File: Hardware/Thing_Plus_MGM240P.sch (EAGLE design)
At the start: 92 parts, among them J1 THING_PLUS_LOGICAL, J2 USB Female Type C Connector, J3 QWIIC_RIGHT_ANGLE, J5 MICRO-SDFRICTION, Q1 20V/4.2A/52mΩ/1.4W, U1 MGM240P, U2 XC6222B331MR-G, U3 EFM32GG12B410F1024GL120, U4 MCP73831, U5 MAX17048, U6 M24C02-FMC6TG, U7 MX25R8035FZUIL0, Y1 CRYSTAL-48MHZ

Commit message: Change debugger power circuitry
Remove VDDJ jumper
Remove VDDJ net and replace with 3V3
Add DBG_WAKE net and circuitry, which controls sleep state of debugger chip
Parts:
- removed VDDJ_EN: JUMPER-SMT_2_NC_TRACE_SILK, SparkFun-Jumpers:JUMPER-SMT_2_NC_TRACE_SILK
- added D8: 120mA/40V/370mV, SparkFun-DiscreteSemi:DIODE-SCHOTTKY-RB751S40
- added R18: 1k, SparkFun-Resistors:1KOHM-0402T-1/16W-1%
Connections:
- removed net VDDJ: C18.1, C19.1, C20.1, C21.1, C4.1, C5.1, C6.1, FB1.2, R1.2, R12.2, R14.2, R16.2, R17.2, TP1.1, U3D.DVDD, U3D.IOVDD0, U3D.IOVDD1, U6.VCC, U7.VCC, U7.WP, VDDJ_EN.1
- new net DBG_WAKE: D8.A, U3A.PA5, U3A.PA6
- net 3.3V: now also C18.1, C19.1, C20.1, C21.1, C4.1, C5.1, C6.1, FB1.2, R1.2, R12.2, R14.2, R16.2, R17.2, TP1.1, U3D.DVDD, U3D.IOVDD0, U3D.IOVDD1, U6.VCC, U7.VCC, U7.WP; no longer VDDJ_EN.2
- net GND: now also R18.1
- net V_USB: now also D8.C, R18.2
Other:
- note removed: "Cut trace to disabled debugger chip"

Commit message: Design review updates
Remove VDDJ label from silk
Add jumper to debugger power control circuit for USB battery applications
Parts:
- added LP: JUMPER-SMT_2_NC_TRACE_SILK, SparkFun-Jumpers:JUMPER-SMT_2_NC_TRACE_SILK
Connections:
- new net N$24: D8.C, LP.1, R18.2
- net DBG_WAKE: no longer U3A.PA5
- net V_USB: now also LP.2; no longer D8.C, R18.2
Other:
- note added: "Cut trace to force debugger into low power mode"
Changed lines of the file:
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@@
 <part name="SUPPLY53" library="SparkFun-PowerSymbols" deviceset="3.3V" device=""/>
 <part name="SUPPLY54" library="SparkFun-PowerSymbols" deviceset="3.3V" device=""/>
+<part name="LP" library="SparkFun-Jumpers" deviceset="JUMPER-SMT_2_NC_TRACE" device="_SILK" package3d_urn="urn:adsk.eagle:package:39281/1"/>
 </parts>
 <sheets>
@@
 <wire x1="88.9" y1="55.88" x2="88.9" y2="0" width="0.2032" layer="97" style="longdash"/>
 <wire x1="170.18" y1="55.88" x2="170.18" y2="0" width="0.2032" layer="97" style="longdash"/>
+<text x="312.42" y="195.58" size="2.032" layer="97" font="vector" align="center">Cut trace to force
+debugger into low
+power mode</text>
 </plain>
 <instances>
@@
 <attribute name="VALUE" x="298.704" y="177.8" size="1.778" layer="96" font="vector" rot="R90" align="top-center"/>
 </instance>
-<instance part="SUPPLY22" gate="G$1" x="297.18" y="187.96" smashed="yes">
-<attribute name="VALUE" x="297.18" y="190.754" size="1.778" layer="96" align="bottom-center"/>
+<instance part="SUPPLY22" gate="G$1" x="297.18" y="200.66" smashed="yes">
+<attribute name="VALUE" x="297.18" y="203.454" size="1.778" layer="96" align="bottom-center"/>
 </instance>
 <instance part="GND50" gate="1" x="297.18" y="167.64" smashed="yes">
@@
 <instance part="SUPPLY54" gate="G$1" x="218.44" y="30.48" smashed="yes">
 <attribute name="VALUE" x="218.44" y="33.274" size="1.778" layer="96" align="bottom-center"/>
+</instance>
+<instance part="LP" gate="G$1" x="297.18" y="193.04" smashed="yes" rot="R90">
+<attribute name="NAME" x="294.132" y="193.04" size="1.778" layer="95" font="vector" rot="R90" align="center"/>
 </instance>
 </instances>
@@
 </segment>
 <segment>
-<pinref part="R18" gate="G$1" pin="2"/>
-<wire x1="297.18" y1="182.88" x2="297.18" y2="185.42" width="0.1524" layer="91"/>
-<pinref part="D8" gate="G$1" pin="C"/>
-<wire x1="297.18" y1="185.42" x2="299.72" y2="185.42" width="0.1524" layer="91"/>
+<pinref part="LP" gate="G$1" pin="2"/>
 <pinref part="SUPPLY22" gate="G$1" pin="V_USB"/>
-<wire x1="297.18" y1="185.42" x2="297.18" y2="187.96" width="0.1524" layer="91"/>
-<junction x="297.18" y="185.42"/>
+<wire x1="297.18" y1="198.12" x2="297.18" y2="200.66" width="0.1524" layer="91"/>
 </segment>
 </net>
@@
 <net name="DBG_WAKE" class="0">
 <segment>
-<pinref part="U3" gate="A" pin="PA5"/>
-<wire x1="111.76" y1="104.14" x2="109.22" y2="104.14" width="0.1524" layer="91"/>
-<label x="109.22" y="104.14" size="1.27" layer="95" font="vector" rot="R180" xref="yes"/>
-</segment>
-<segment>
 <pinref part="D8" gate="G$1" pin="A"/>
 <wire x1="304.8" y1="185.42" x2="307.34" y2="185.42" width="0.1524" layer="91"/>
@@
 </segment>
 </net>
+<net name="N$24" class="0">
+<segment>
+<pinref part="R18" gate="G$1" pin="2"/>
+<pinref part="LP" gate="G$1" pin="1"/>
+<wire x1="297.18" y1="182.88" x2="297.18" y2="185.42" width="0.1524" layer="91"/>
+<pinref part="D8" gate="G$1" pin="C"/>
+<wire x1="297.18" y1="185.42" x2="297.18" y2="187.96" width="0.1524" layer="91"/>
+<wire x1="299.72" y1="185.42" x2="297.18" y2="185.42" width="0.1524" layer="91"/>
+<junction x="297.18" y="185.42"/>
+</segment>
+</net>

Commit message: Testing fixes
Update version number to v02
Mirror MX8035 footprint (whoops...)
Swap R15 for 2k2 (turns out VREGO is 3V3, not 5V)
Add trace to 3V3 pour to connect between V_USB and N$24
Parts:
- R15: value 4.7k -> 2.2k; device SparkFun-Resistors:4.7KOHM-0402T-1/16W-1% -> SparkFun-Resistors:2.2KOHM-0402T-1/16W-1%
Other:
- note added: "v02"
- note removed: "v01"
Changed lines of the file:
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@@
 <part name="SUPPLY34" library="SparkFun-PowerSymbols" deviceset="V_USB" device=""/>
 <part name="D6" library="SparkFun-LED" deviceset="LED-BLUE" device="0603" value="BLUE"/>
-<part name="R15" library="SparkFun-Resistors" deviceset="4.7KOHM" device="-0402T-1/16W-1%" value="4.7k"/>
+<part name="R15" library="SparkFun-Resistors" deviceset="2.2KOHM" device="-0402T-1/16W-1%" value="2.2k"/>
 <part name="C11" library="SparkFun-Capacitors" deviceset="1.0UF" device="-0402T-16V-10%" value="1.0uF"/>
 <part name="C12" library="SparkFun-Capacitors" deviceset="4.7UF" device="-0402_TIGHT-6.3V-20%-X5R" value="4.7uF"/>
@@
 <wire x1="99.06" y1="149.86" x2="0" y2="149.86" width="0.2032" layer="97" style="longdash"/>
 <text x="358.14" y="12.7" size="2.54" layer="94" font="vector" align="center">Dryw Wade</text>
-<text x="424.18" y="7.62" size="2.54" layer="94" font="vector" align="center">v01</text>
+<text x="424.18" y="7.62" size="2.54" layer="94" font="vector" align="center">v02</text>
 <text x="20.32" y="205.74" size="2.032" layer="97" font="vector" rot="R180" align="center">Cut trace to
 remove power LED</text>

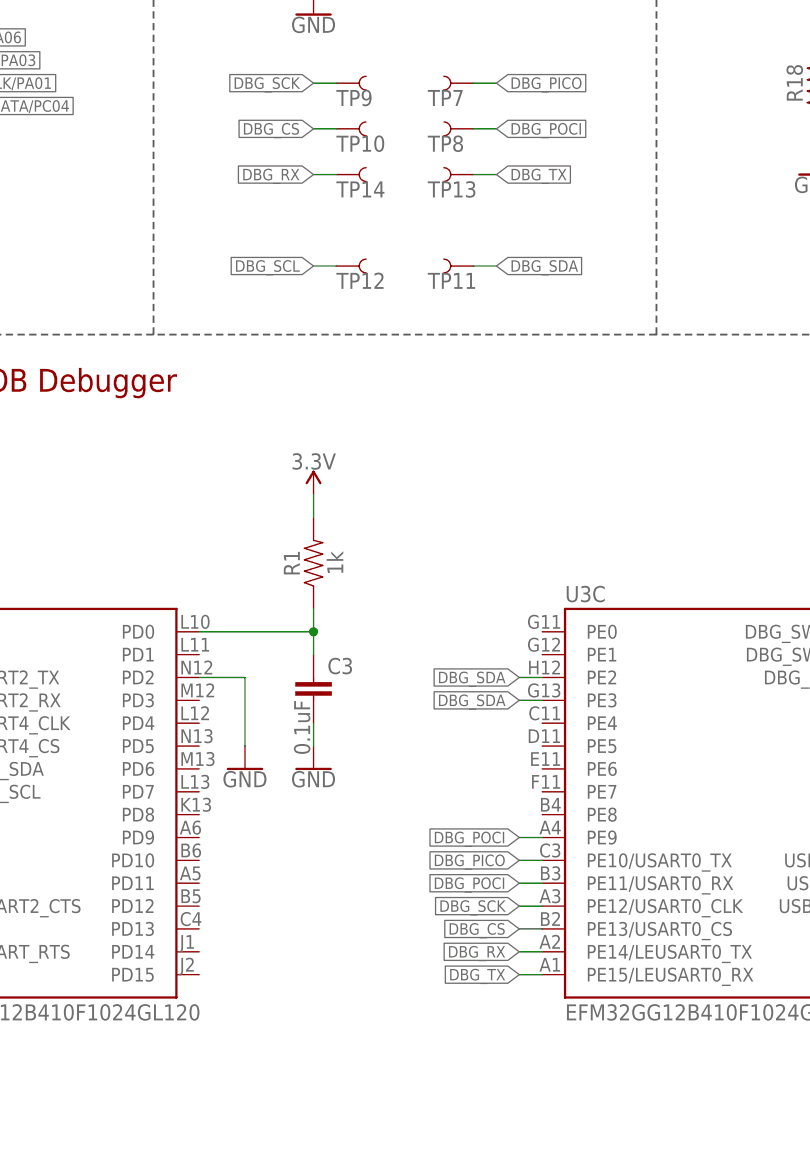
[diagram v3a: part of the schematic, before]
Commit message: Flip DBG TX and RX
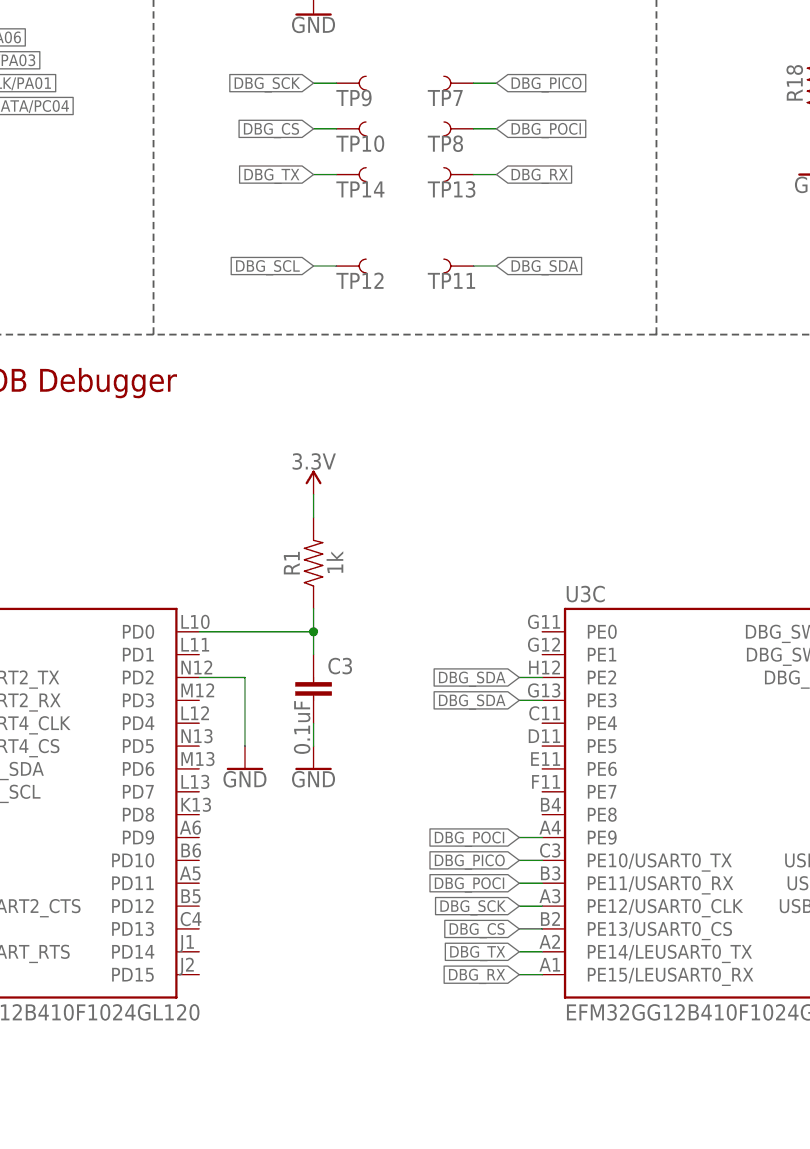
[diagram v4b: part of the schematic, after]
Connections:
- net DBG_RX: now also TP13.1, U3C.PE15/LEUSART0_RX; no longer TP14.1, U3C.PE14/LEUSART0_TX
- net DBG_TX: now also TP14.1, U3C.PE14/LEUSART0_TX; no longer TP13.1, U3C.PE15/LEUSART0_RX
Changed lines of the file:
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@@
 </segment>
 </net>
-<net name="DBG_TX" class="0">
+<net name="DBG_RX" class="0">
 <segment>
 <pinref part="U3" gate="C" pin="PE15/LEUSART0_RX"/>
@@
 </segment>
 </net>
-<net name="DBG_RX" class="0">
+<net name="DBG_TX" class="0">
 <segment>
 <pinref part="U3" gate="C" pin="PE14/LEUSART0_TX"/>

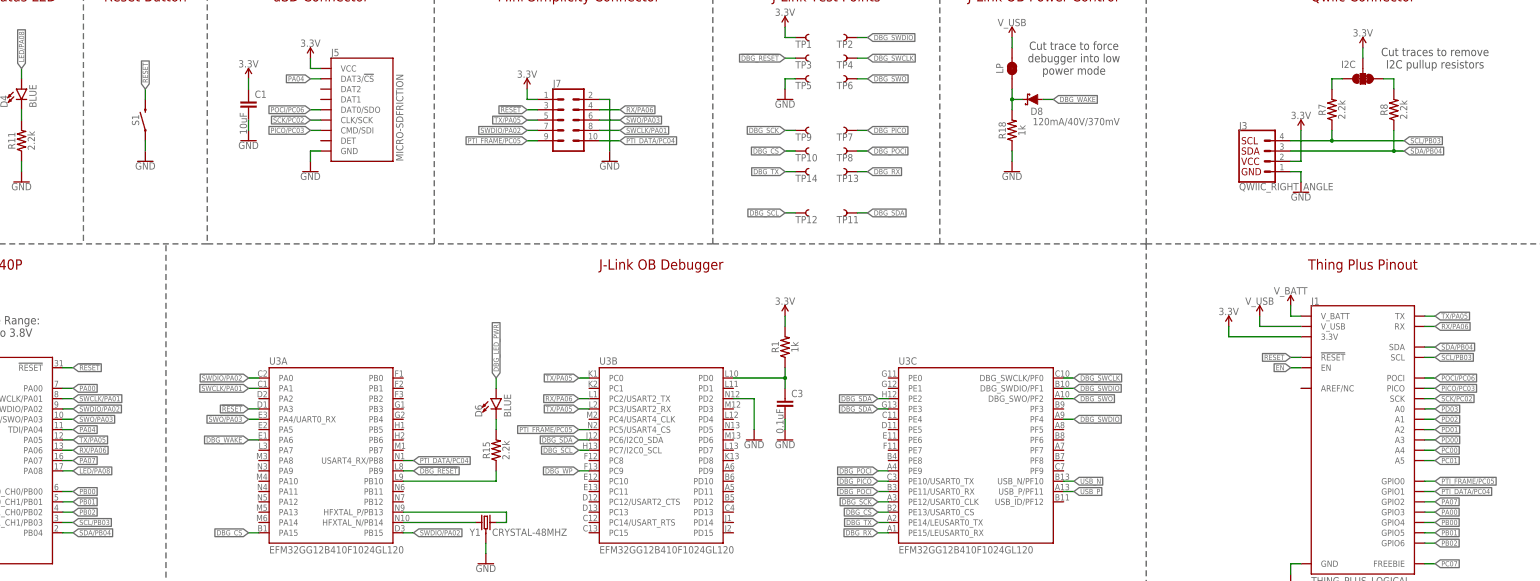
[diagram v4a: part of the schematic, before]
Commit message: Swap PA04 and PA07
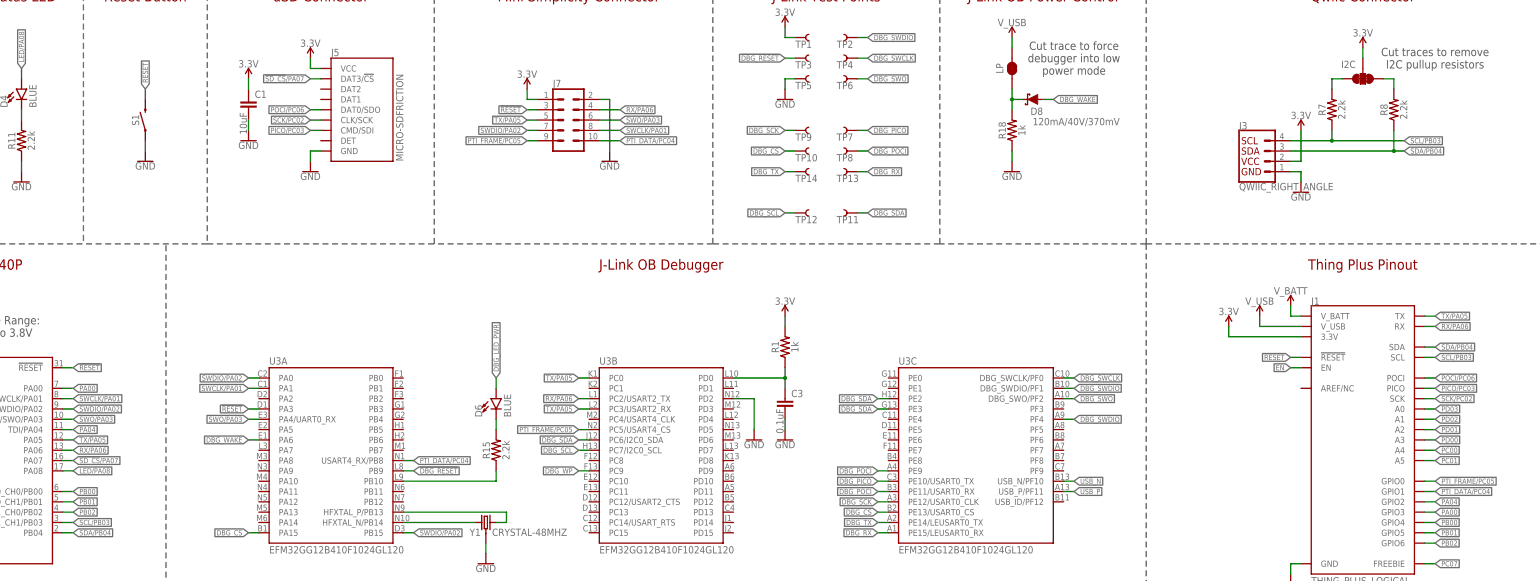
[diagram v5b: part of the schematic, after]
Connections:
- removed net PA07: J1.GPIO2, U1.PA07
- new net !SD_CS!/PA07: J5.DAT3/!CS!, U1.PA07
- net PA04: now also J1.GPIO2; no longer J5.DAT3/!CS!
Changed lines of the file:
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@@
 </segment>
 <segment>
-<pinref part="J5" gate="J1" pin="DAT3/!CS!"/>
-<wire x1="127" y1="190.5" x2="124.46" y2="190.5" width="0.1524" layer="91"/>
-<label x="124.46" y="190.5" size="1.27" layer="95" font="vector" rot="R180" xref="yes"/>
+<pinref part="J1" gate="G$1" pin="GPIO2"/>
+<wire x1="398.78" y1="86.36" x2="401.32" y2="86.36" width="0.1524" layer="91"/>
+<label x="401.32" y="86.36" size="1.27" layer="95" font="vector" xref="yes"/>
 </segment>
 </net>
@@
 </segment>
 </net>
-<net name="PA07" class="0">
-<segment>
-<pinref part="J1" gate="G$1" pin="GPIO2"/>
-<wire x1="398.78" y1="86.36" x2="401.32" y2="86.36" width="0.1524" layer="91"/>
-<label x="401.32" y="86.36" size="1.27" layer="95" font="vector" xref="yes"/>
-</segment>
+<net name="!SD_CS!/PA07" class="0">
 <segment>
 <pinref part="U1" gate="G$1" pin="PA07"/>
@@
 <label x="66.04" y="96.52" size="1.27" layer="95" font="vector" xref="yes"/>
 </segment>
+<segment>
+<pinref part="J5" gate="J1" pin="DAT3/!CS!"/>
+<wire x1="127" y1="190.5" x2="124.46" y2="190.5" width="0.1524" layer="91"/>
+<label x="124.46" y="190.5" size="1.27" layer="95" font="vector" rot="R180" xref="yes"/>
+</segment>
 </net>

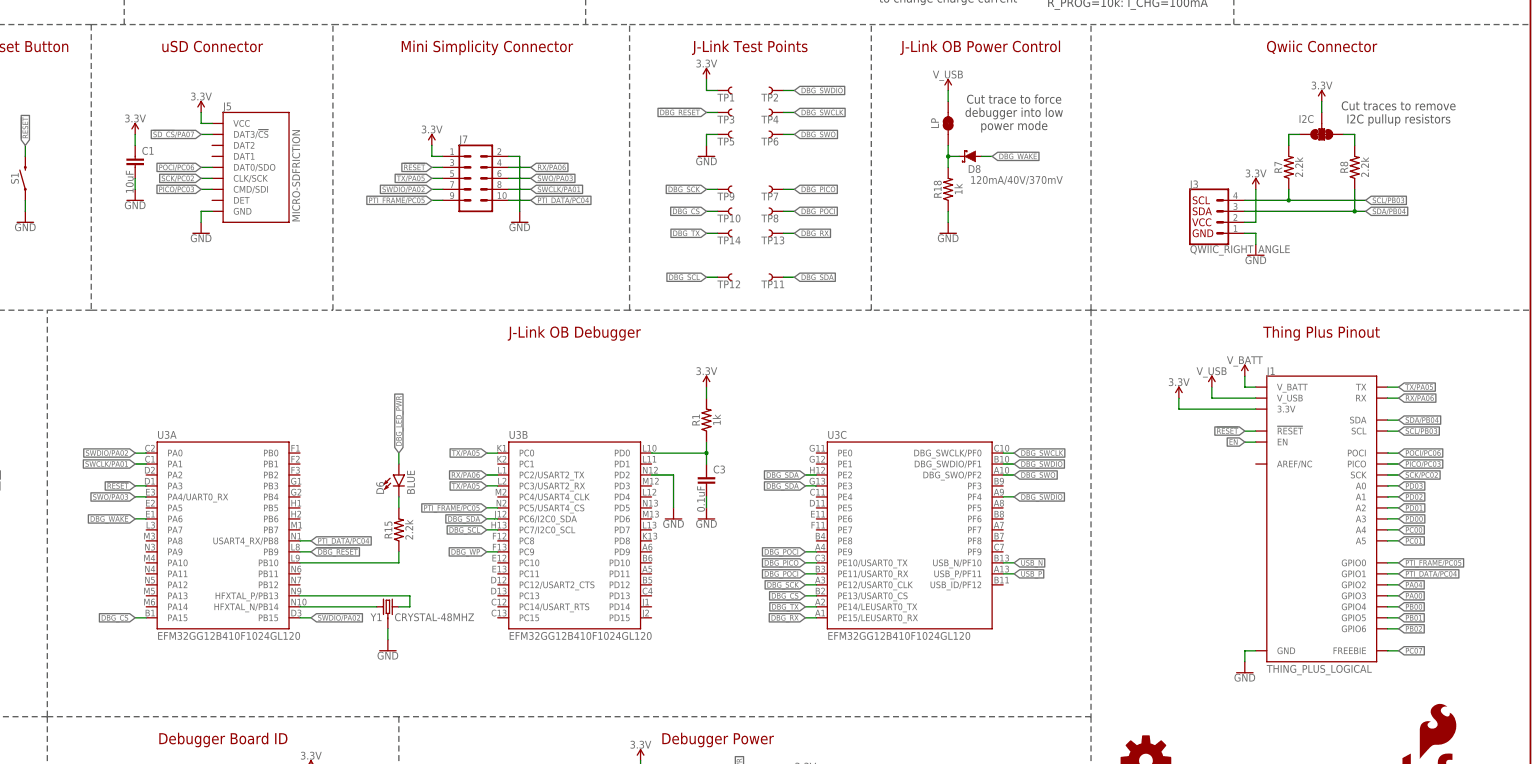
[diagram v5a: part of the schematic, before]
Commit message: Design review updates
Add GND vias along antenna cutout edge
Add extra GND vias near MGM240P GND pads
Add pullup resistor to SD card CS pin
Add extra GND vias between I2C and SPI traces on bottom
Widen DECOUPLE trace
Add series resistors to MGM240P's RX inputs to prevent contention between debugger, Mini Simplicity connector, and Thing Plus RX pin
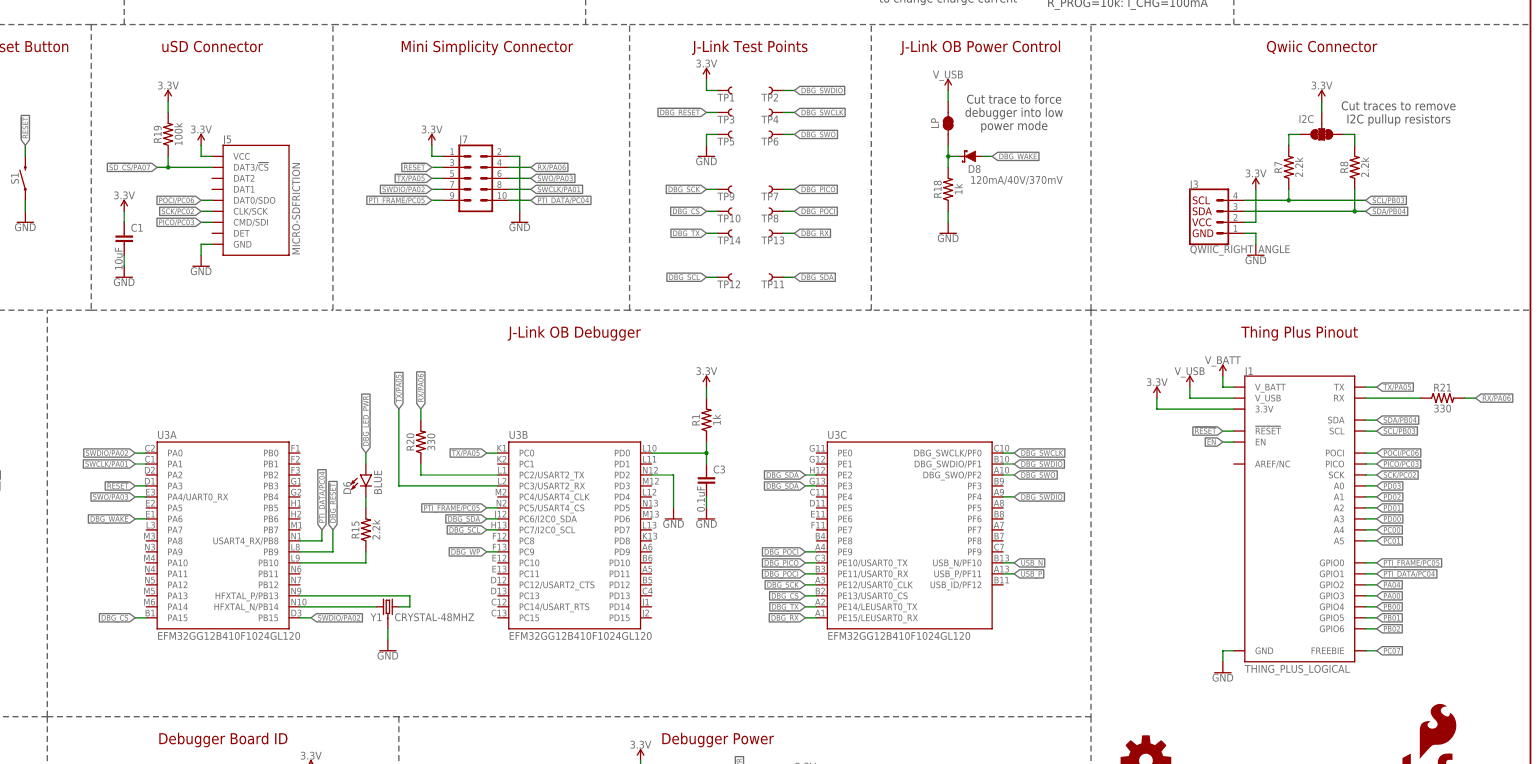
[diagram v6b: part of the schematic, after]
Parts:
- added R19: 100k, SparkFun-Resistors:100KOHM-0402T-1/16W-1%
- added R20, R21: 330, SparkFun-Resistors:330OHM-0402T-1/16W-5%
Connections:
- new net N$25: R20.1, U3B.PC2/USART2_TX
- new net N$26: J1.RX, R21.1
- net !SD_CS!/PA07: now also R19.1
- net 3.3V: now also R19.2
- net RX/PA06: now also R20.2, R21.2; no longer J1.RX, U3B.PC2/USART2_TX
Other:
- moved on the sheet: C1, D6, J1, J5, R15
